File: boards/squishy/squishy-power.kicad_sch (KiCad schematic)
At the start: 62 parts, among them SW1 RST, U1 LFE5UM5G-45F-8BG381C, U10 TPS720115QDRVRQ1, U16 LP5910-1.8DRVR, U2 GD25Q64EWIGR, U5 APX811-40UG-7, U7 TPS73733DRVR, U8 TPS7A1125PDRVT, U9 TPS7A1112PDRVT

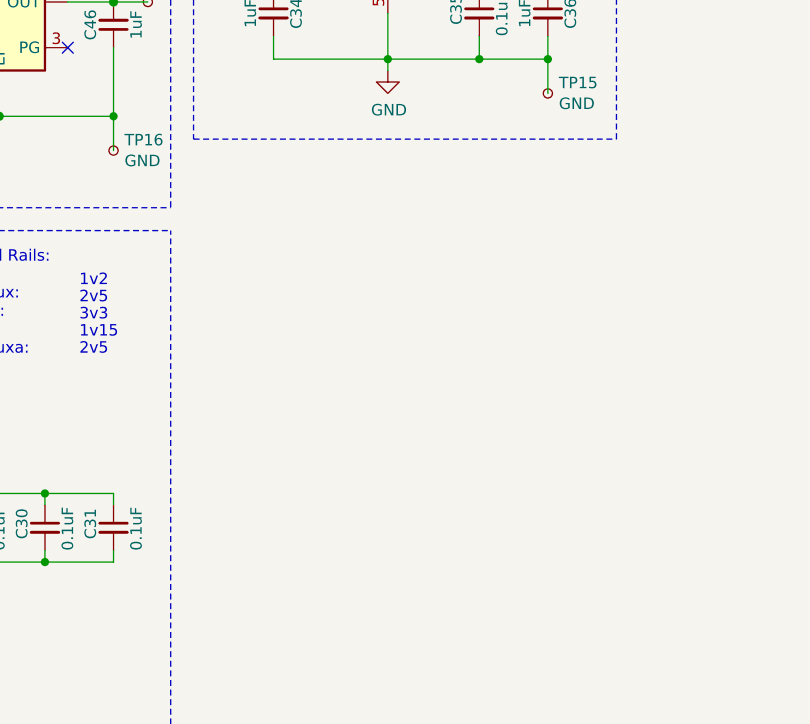
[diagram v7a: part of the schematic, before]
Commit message: hardware: squishy: some hyperram stuff and library updates
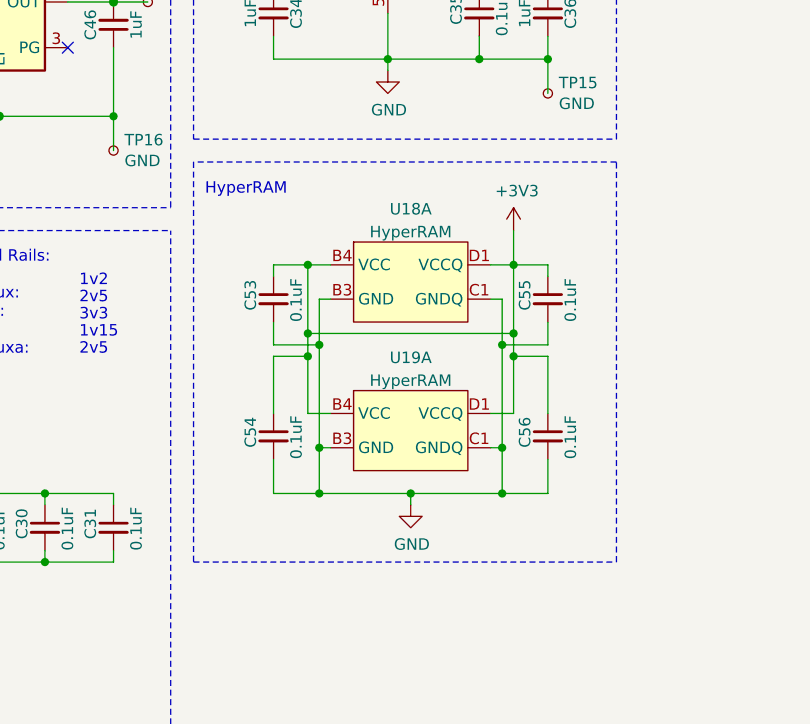
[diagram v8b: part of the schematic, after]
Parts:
- added C53, C54, C55, C56: 0.1uF, Capacitor_SMD:C_0402_1005Metric, symbol Device:C_Small
- added U18, U19: HyperRAM, lethalbit-memory:TFBGA-24-6x8mm-1.0mm, symbol lethalbit-memory:HyperRAM
- U2: footprint Package_SON:WSON-8-1EP_6x5mm_P1.27mm_EP3.4x4mm -> rhais_package-qfn:UDFN-8-1EP_6x5mm_P1.27mm_EP3.4x4mm
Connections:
- net +3V3: now also C53.1, C54.1, C55.1, C56.1, U18.B4 (VCC), U18.D1 (VCCQ), U18.E4 (VCCQ), U19.B4 (VCC), U19.D1 (VCCQ), U19.E4 (VCCQ)
- net GND: now also C53.2, C54.2, C55.2, C56.2, U18.B3 (GND), U18.C1 (GNDQ), U18.E5 (GNDQ), U19.B3 (GND), U19.C1 (GNDQ), U19.E5 (GNDQ)
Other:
- note added: "HyperRAM"
